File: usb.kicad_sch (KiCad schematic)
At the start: 11 parts, among them Con5 USB_C_Wurth_632723130112, U8 USBLC6-2, U9 USBLC6-2

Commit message: Tracking finished
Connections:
- net USB-C-ID: no longer Con5.B3 (SSTXN2-)
- no-connect marks 9 -> 10
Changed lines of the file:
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@@
   )
   (junction (at 166.37 95.25) (diameter 1.016) (color 0 0 0 0))
-  (junction (at 205.74 100.33) (diameter 1.016) (color 0 0 0 0))
+  (junction (at 205.74 99.06) (diameter 1.016) (color 0 0 0 0))
   (junction (at 214.63 88.9) (diameter 1.016) (color 0 0 0 0))
   (junction (at 214.63 90.17) (diameter 1.016) (color 0 0 0 0))
   (junction (at 214.63 91.44) (diameter 1.016) (color 0 0 0 0))
-  (junction (at 214.63 100.33) (diameter 1.016) (color 0 0 0 0))
   (junction (at 214.63 107.95) (diameter 1.016) (color 0 0 0 0))
   (junction (at 214.63 113.03) (diameter 1.016) (color 0 0 0 0))
@@
   (no_connect (at 217.17 134.62))
   (no_connect (at 217.17 137.16))
+  (no_connect (at 217.17 142.24))
   (no_connect (at 217.17 144.78))
   (no_connect (at 217.17 149.86))
@@
     (stroke (width 0) (type solid) (color 0 0 0 0))
   )
-  (wire (pts (xy 205.74 100.33) (xy 205.74 95.25))
+  (wire (pts (xy 205.74 95.25) (xy 205.74 99.06))
     (stroke (width 0) (type solid) (color 0 0 0 0))
   )
-  (wire (pts (xy 205.74 142.24) (xy 205.74 100.33))
+  (wire (pts (xy 205.74 99.06) (xy 217.17 99.06))
+    (stroke (width 0) (type solid) (color 0 0 0 0))
+  )
+  (wire (pts (xy 205.74 101.6) (xy 205.74 99.06))
     (stroke (width 0) (type solid) (color 0 0 0 0))
   )
@@
     (stroke (width 0) (type solid) (color 0 0 0 0))
   )
-  (wire (pts (xy 214.63 99.06) (xy 214.63 100.33))
-    (stroke (width 0) (type solid) (color 0 0 0 0))
-  )
-  (wire (pts (xy 214.63 100.33) (xy 205.74 100.33))
-    (stroke (width 0) (type solid) (color 0 0 0 0))
-  )
-  (wire (pts (xy 214.63 100.33) (xy 214.63 101.6))
-    (stroke (width 0) (type solid) (color 0 0 0 0))
-  )
-  (wire (pts (xy 214.63 101.6) (xy 217.17 101.6))
-    (stroke (width 0) (type solid) (color 0 0 0 0))
-  )
   (wire (pts (xy 214.63 106.68) (xy 214.63 107.95))
     (stroke (width 0) (type solid) (color 0 0 0 0))
@@
     (stroke (width 0) (type solid) (color 0 0 0 0))
   )
-  (wire (pts (xy 217.17 99.06) (xy 214.63 99.06))
+  (wire (pts (xy 217.17 101.6) (xy 205.74 101.6))
     (stroke (width 0) (type solid) (color 0 0 0 0))
   )
@@
     (stroke (width 0) (type solid) (color 0 0 0 0))
   )
-  (wire (pts (xy 217.17 142.24) (xy 205.74 142.24))
-    (stroke (width 0) (type solid) (color 0 0 0 0))
-  )

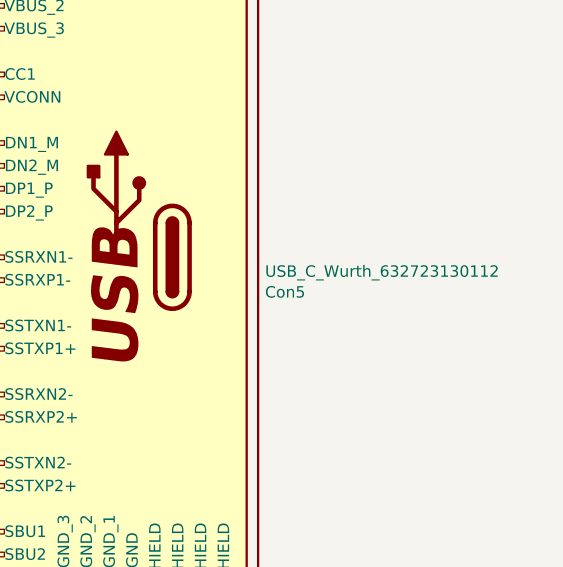
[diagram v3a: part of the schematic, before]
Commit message: Make all connections, started track tunning
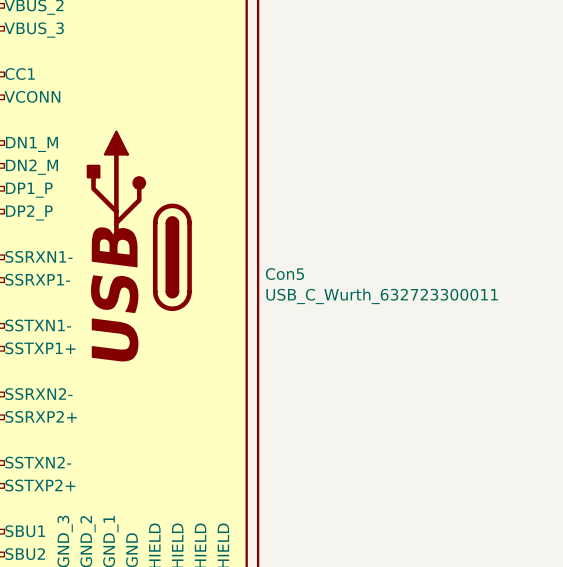
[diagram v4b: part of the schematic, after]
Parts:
- removed Con5: USB_C_Wurth_632723130112, Connector_USB:USB_C_632723130112, symbol USB_Connectors:USB_C_Wurth_632723130112
- added Con5: USB_C_Wurth_632723300011, Connector_USB:632723300011, symbol USB_Connectors:USB_C_Wurth_632723300011
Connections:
- net 5V: now also Con5.A4 (VBUS), Con5.A9 (VBUS_1), Con5.B4 (VBUS_2), Con5.B9 (VBUS_3)
- net GND: now also Con5.A1 (GND), Con5.A12 (GND_1), Con5.B1 (GND_2), Con5.B12 (GND_3)
- net USB-C-ID: now also Con5.A5 (CC1), Con5.B5 (VCONN)
- net at U8.4: now also Con5.A6 (DP1_P), Con5.B6 (DP2_P)
- net at U8.6: now also Con5.A7 (DN1_M), Con5.B7 (DN2_M)
- net at C49.2: now also Con5.S1 (SHIELD), Con5.S2 (SHIELD), Con5.S3 (SHIELD), Con5.S4 (SHIELD)
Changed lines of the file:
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@@
     (pin "6")
   )
-  (symbol (lib_id "USB_Connectors:USB_C_Wurth_632723130112") (at 236.22 119.38 0) (mirror y) (unit 1)
-    (in_bom yes) (on_board yes)
-    (property "Reference" "Con5" (id 0) (at 252.222 123.2662 0)
+  (symbol (lib_id "USB_Connectors:USB_C_Wurth_632723300011") (at 236.22 119.38 0) (mirror y) (unit 1)
+    (in_bom yes) (on_board yes) (fields_autoplaced)
+    (property "Reference" "Con5" (id 0) (at 252.2221 121.2861 0)
       (effects (font (size 1.27 1.27)) (justify right))
     )
-    (property "Value" "USB_C_Wurth_632723130112" (id 1) (at 252.222 120.9548 0)
+    (property "Value" "USB_C_Wurth_632723300011" (id 1) (at 252.2221 123.5848 0)
       (effects (font (size 1.27 1.27)) (justify right))
     )
-    (property "Footprint" "Connector_USB:USB_C_632723130112" (id 2) (at 234.95 116.84 0)
+    (property "Footprint" "Connector_USB:632723300011" (id 2) (at 234.95 116.84 0)
       (effects (font (size 1.27 1.27)) hide)
     )
-    (property "Datasheet" "https://www.we-online.com/catalog/datasheet/632723130112.pdf" (id 3) (at 234.95 116.84 0)
+    (property "Datasheet" "https://pl.mouser.com/datasheet/2/445/632723300011-1718173.pdf" (id 3) (at 234.95 116.84 0)
       (effects (font (size 1.27 1.27)) hide)
     )
@@
       (effects (font (size 1.27 1.27)) hide)
     )
-    (property "Manufacturer Part Number" "632723130112" (id 5) (at 234.95 119.38 0)
+    (property "Manufacturer Part Number" "632723300011" (id 5) (at 234.95 119.38 0)
       (effects (font (size 1.27 1.27)) hide)
     )
@@
       (effects (font (size 1.27 1.27)) hide)
     )
-    (property "Supplier Part Number" "710-632723130112" (id 7) (at 234.95 119.38 0)
+    (property "Supplier Part Number" "710-632723300011" (id 7) (at 234.95 119.38 0)
       (effects (font (size 1.27 1.27)) hide)
     )
-    (property "URL" "https://pl.mouser.com/ProductDetail/Wurth-Elektronik/632723130112?qs=2WXlatMagcEknienHxbwUw%3D%3D" (id 8) (at 234.95 119.38 0)
+    (property "URL" "https://pl.mouser.com/ProductDetail/Wurth-Elektronik/632723300011?qs=NK6InXoXhq4%252B5eM1PePLPg%3D%3D" (id 8) (at 234.95 119.38 0)
       (effects (font (size 1.27 1.27)) hide)
     )
-    (property "Price@1pc" "21,34" (id 9) (at 234.95 119.38 0)
+    (property "Price@1pc" "17,55" (id 9) (at 234.95 119.38 0)
       (effects (font (size 1.27 1.27)) hide)
     )
-    (property "Price@1000pcs" "13,16" (id 10) (at 234.95 119.38 0)
+    (property "Price@1000pcs" "11,70" (id 10) (at 234.95 119.38 0)
       (effects (font (size 1.27 1.27)) hide)
     )
